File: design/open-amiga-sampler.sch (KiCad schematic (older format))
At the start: 14 parts, among them J1 Audio in, J2 DB25_Male, U1 MCP6002-xP, U2 ADC0820CCN

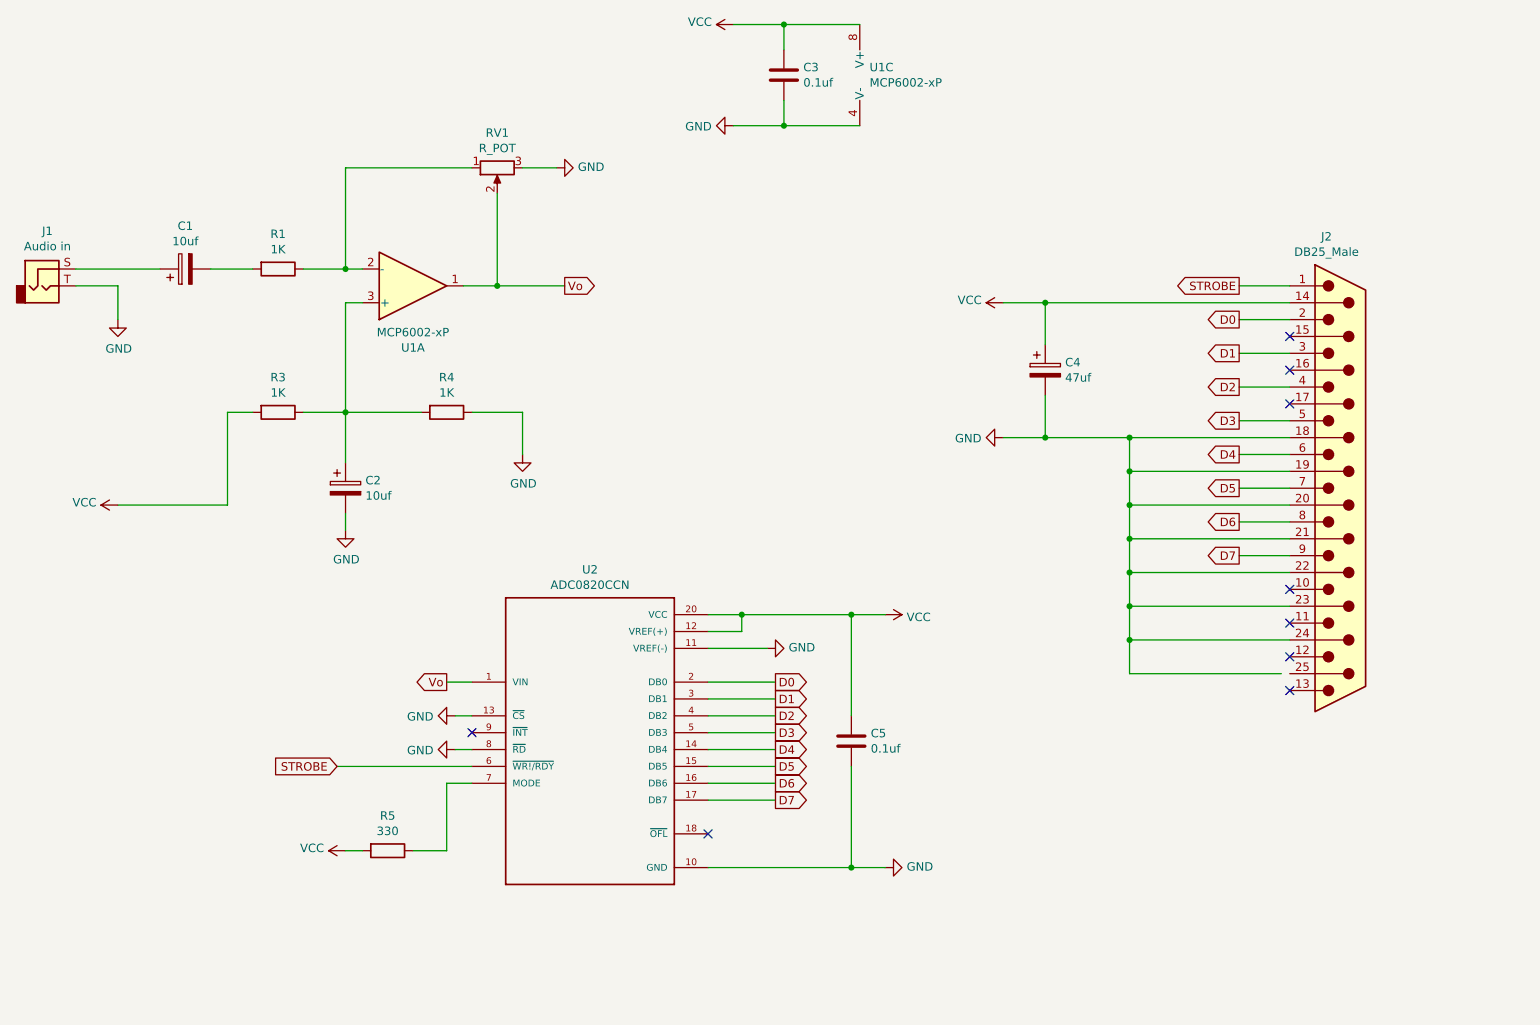
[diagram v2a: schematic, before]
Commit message: Added stereo mix circuit
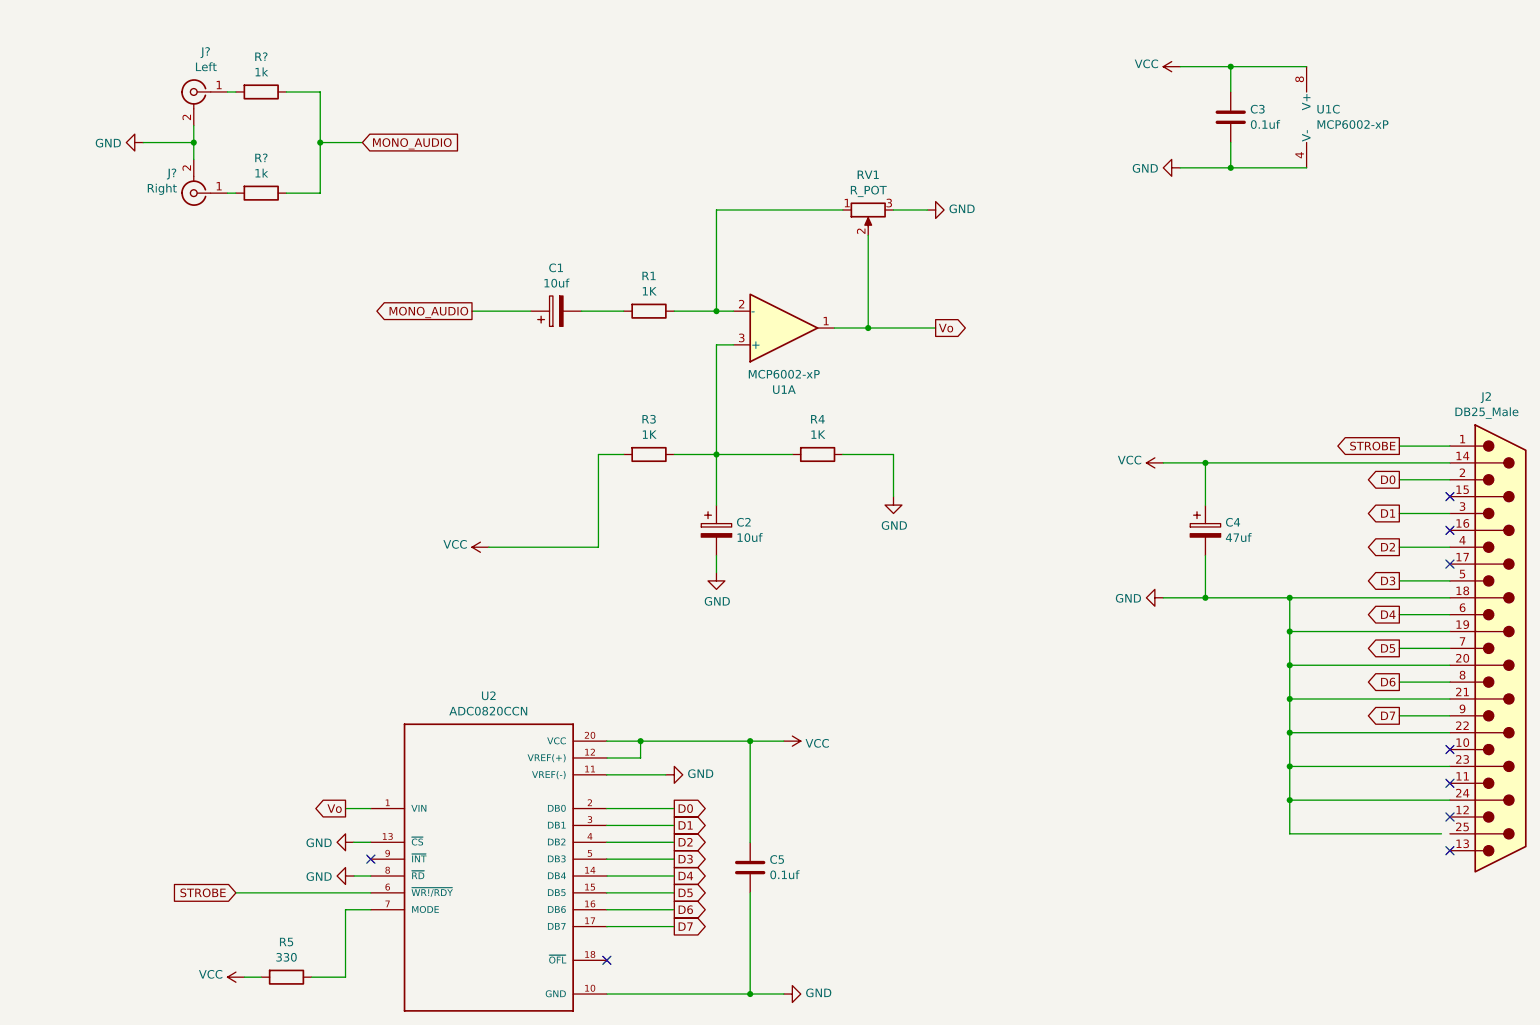
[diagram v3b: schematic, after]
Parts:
- removed J1: Audio in, symbol Connector:AudioJack2
- added J?: Right, symbol Connector:Conn_Coaxial
- added J?: Left, symbol Connector:Conn_Coaxial
- added R? (x2): 1k, symbol Device:R
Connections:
- net GND: now also J?.2 (Ext), J?.2 (Ext)
- net MONO_AUDIO: now reaches C1.1
- net MONO_AUDIO: now also R?.1, R?.1
- new net: J?.1 (In), R?.2 (x2)
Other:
- moved on the sheet: C1, C2, C3, C4, C5, J2, R1, R3, R4, R5, RV1, U1A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

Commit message: Initial go at a PCB layout.
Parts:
- C1, C2, C4: footprint (none) -> Capacitor_THT:CP_Radial_D4.0mm_P1.50mm
- C3: renamed from C5; footprint (none) -> Capacitor_THT:C_Disc_D4.3mm_W1.9mm_P5.00mm
- C5: renamed from C3; footprint (none) -> Capacitor_THT:C_Disc_D4.3mm_W1.9mm_P5.00mm
- J1, J2: renamed from J?; footprint (none) -> connectors:Audio pads
- J3: renamed from J2; footprint (none) -> Connector_Dsub:DSUB-25_Male_EdgeMount_P2.77mm
- R1, R2: renamed from R?; footprint (none) -> Resistor_THT:R_Axial_DIN0207_L6.3mm_D2.5mm_P10.16mm_Horizontal
- R3: renamed from R5; footprint (none) -> Resistor_THT:R_Axial_DIN0207_L6.3mm_D2.5mm_P10.16mm_Horizontal
- R4: renamed from R1; footprint (none) -> Resistor_THT:R_Axial_DIN0207_L6.3mm_D2.5mm_P10.16mm_Horizontal
- R5: renamed from R3; footprint (none) -> Resistor_THT:R_Axial_DIN0207_L6.3mm_D2.5mm_P10.16mm_Horizontal
- R6: renamed from R4; footprint (none) -> Resistor_THT:R_Axial_DIN0207_L6.3mm_D2.5mm_P10.16mm_Horizontal
- RV1: footprint (none) -> connectors:Pot pads
- U1: renamed from U2; footprint DIP779W45P254L2641H508Q20 -> Package_DIP:DIP-20_W7.62mm_Socket
- U2: renamed from U1; footprint (none) -> Package_DIP:DIP-8_W7.62mm_Socket
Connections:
- net GND: now also J3.25 (P25)

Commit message: Fixed op amp circuit
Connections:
- net GND: no longer RV1.3
- net Vo: now also RV1.3
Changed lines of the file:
@@
 	0    -1   1    0
-$EndComp
-$Comp
-L power:GND #PWR011
-U 1 1 5F218CFB
-P 6350 2150
-F 0 "#PWR011" H 6350 1900 50  0001 C CNN
-F 1 "GND" V 6355 2022 50  0000 R CNN
-F 2 "" H 6350 2150 50  0001 C CNN
-F 3 "" H 6350 2150 50  0001 C CNN
-	1    6350 2150
-	0    -1   -1   0
 $EndComp
 Wire Wire Line
@@
 	5100 2750 5200 2750
 Wire Wire Line
-	6000 2300 6000 2850
+	6000 2300 6000 2500
 Connection ~ 6000 2850
 Wire Wire Line
@@
 Wire Wire Line
 	9450 5850 8500 5850
+Wire Wire Line
+	6350 2150 6350 2500
+Wire Wire Line
+	6350 2500 6000 2500
+Connection ~ 6000 2500
+Wire Wire Line
+	6000 2500 6000 2850
 $EndSCHEMATC
